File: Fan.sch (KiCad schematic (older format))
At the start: 0 parts

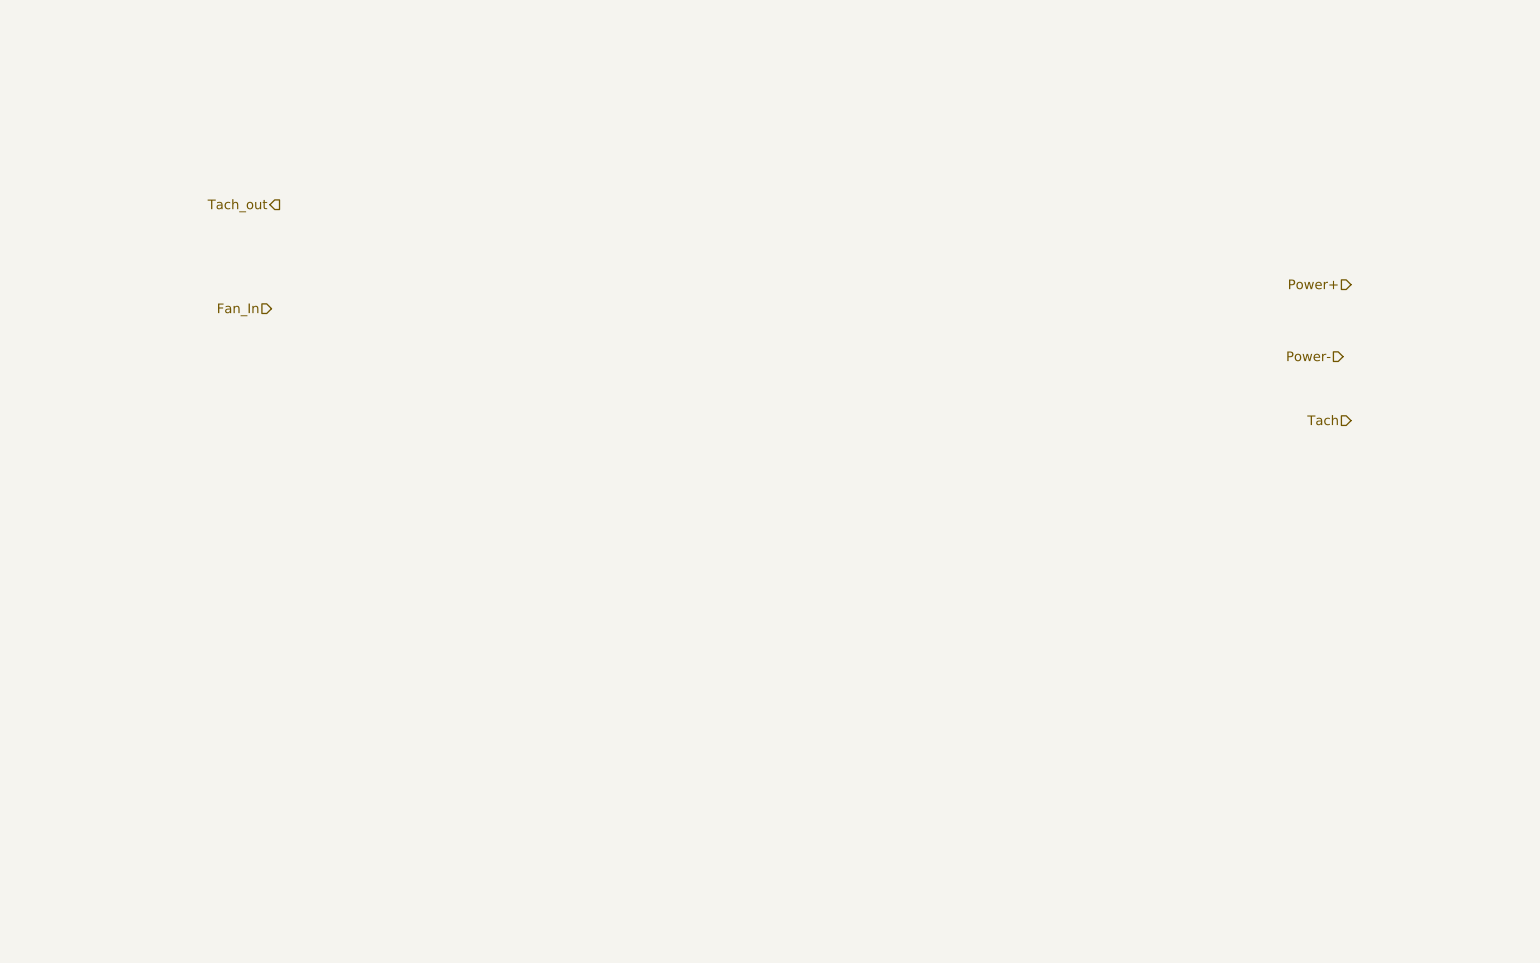
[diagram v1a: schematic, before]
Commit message: Module 3. Unit 4
Create the rough out of the Fan module
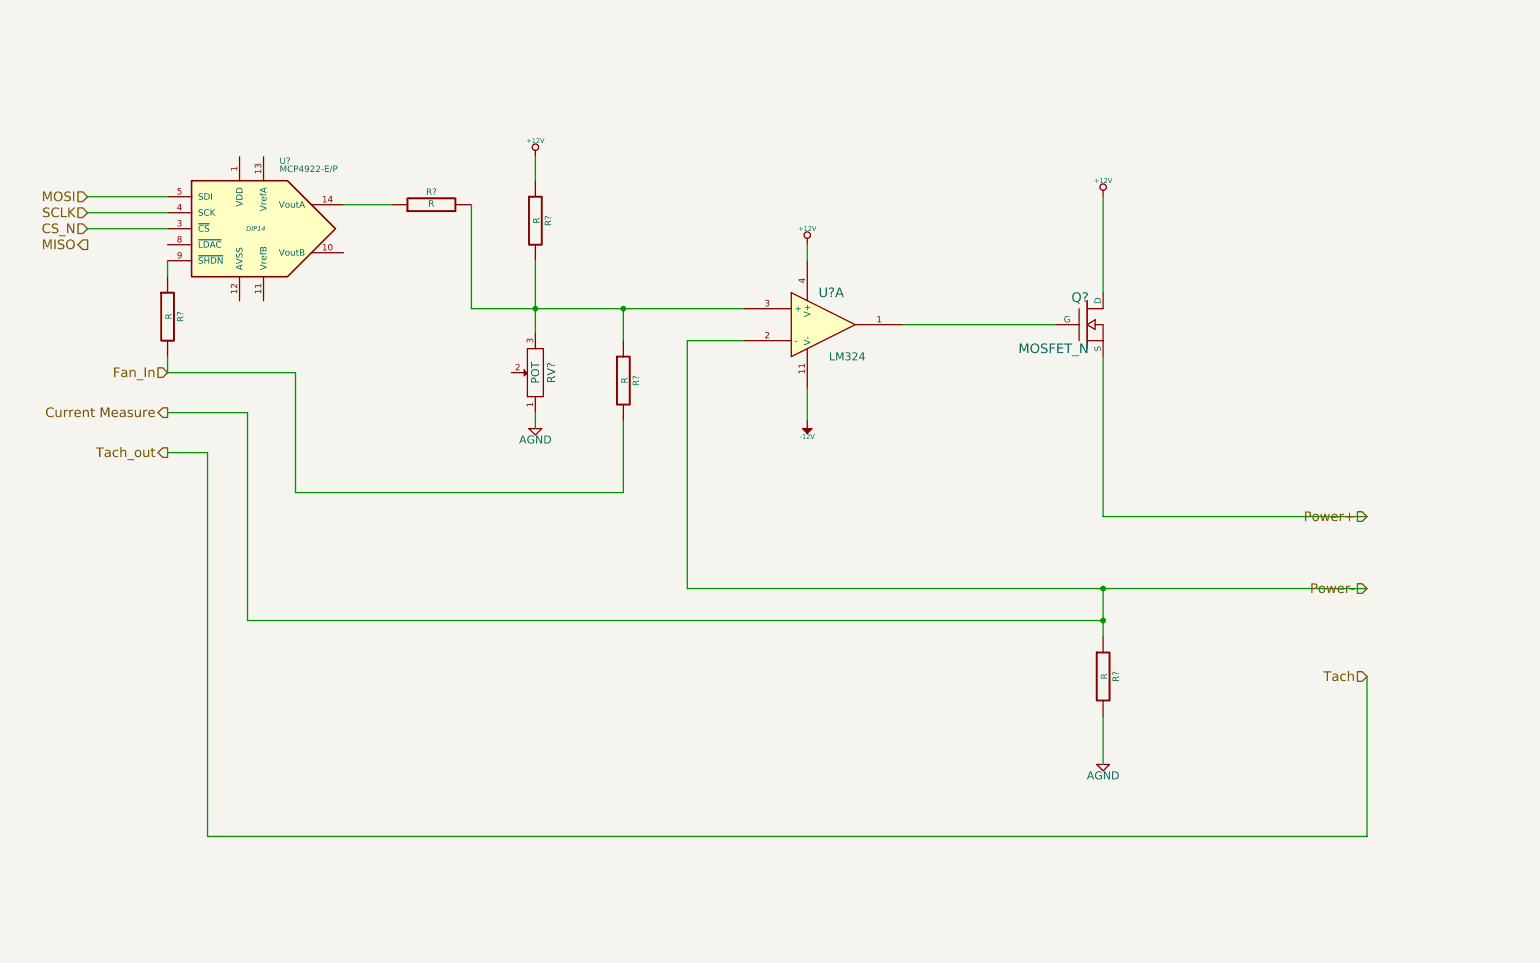
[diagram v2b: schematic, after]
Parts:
- added Q?: MOSFET_N, ~, symbol MOSFET_N
- added R? (x5): R, ~, symbol R
- added RV?: POT, ~, symbol POT
- added U?: LM324, ~, symbol LM324
- added U?: MCP4922-E/P, DIP14, symbol MCP4922-E/P
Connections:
- net Fan_In: now also R?.2, R?.2
- net Power+: now also Q?.S
- new net: Q?.G, U?.1
- new net: R?.1, R?.2, R?.2, RV?.3, U?.3 (+)
- new net: R?.1, U?.14 (VoutA)
- new net: R?.1, U?.9 (~SHDN~)
- new net +12V: Q?.D, R?.1, U?.4 (V+)
- new net -12V: U?.11 (V-)
- new net AGND: R?.2, RV?.1
- new net CS_N: U?.3 (~CS~)
- new net Current Measure: R?.1, U?.2 (-)
- new net MOSI: U?.5 (SDI)
- new net SCLK: U?.4 (SCK)

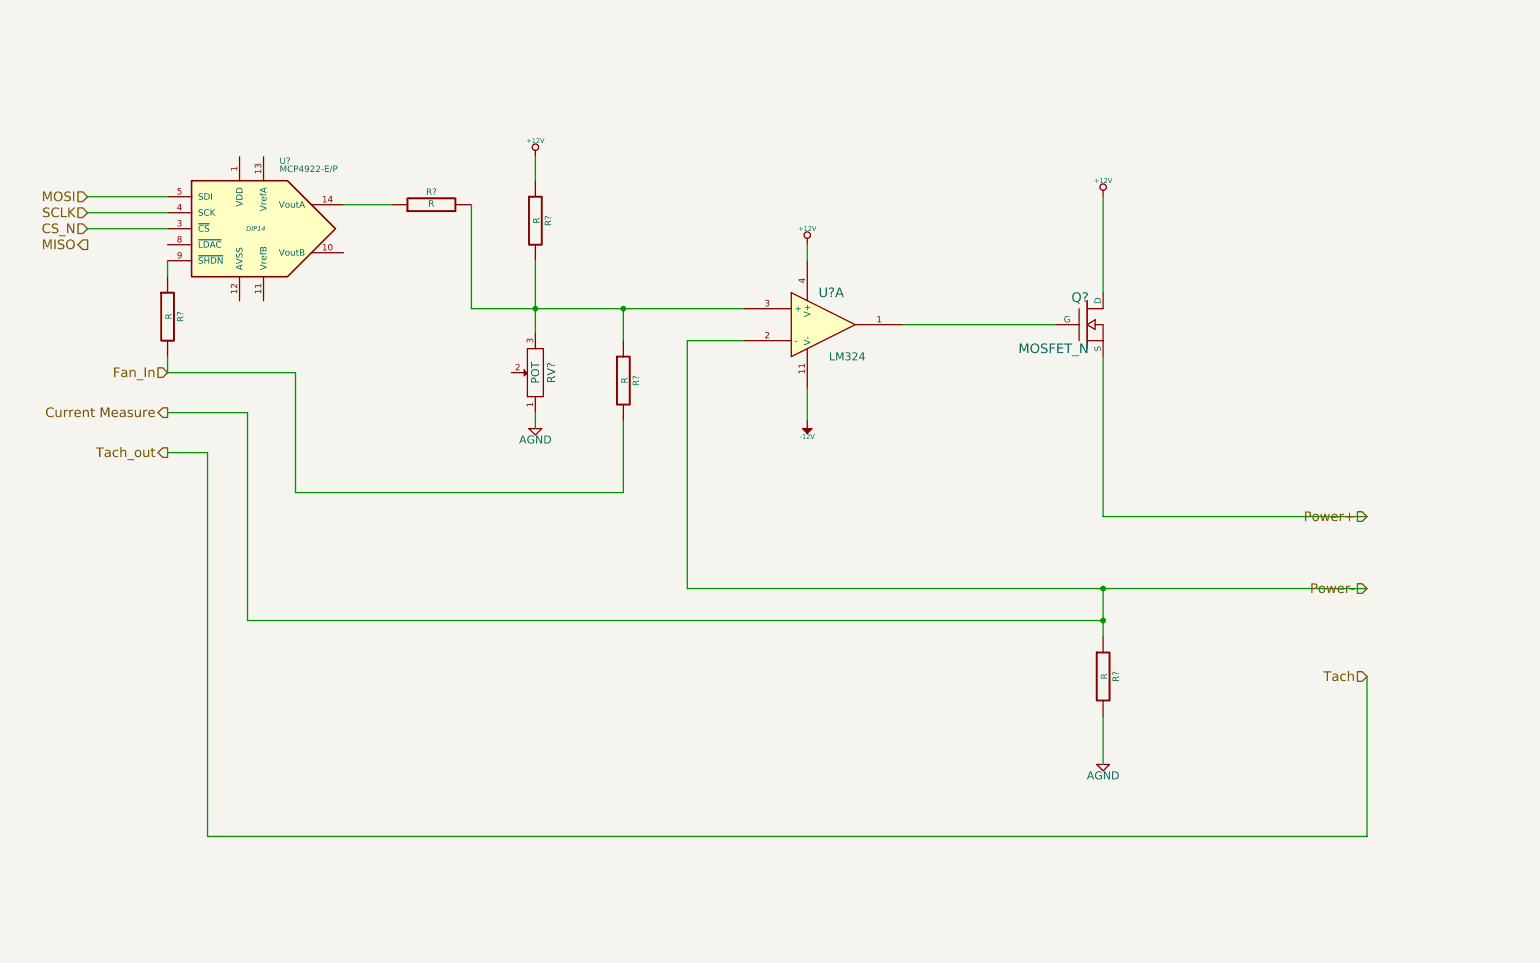
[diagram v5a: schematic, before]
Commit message: M3 U8
Arduino Module.   My Arduino Pin numbering does not matches Chris'.  I
believe he missed one in the video
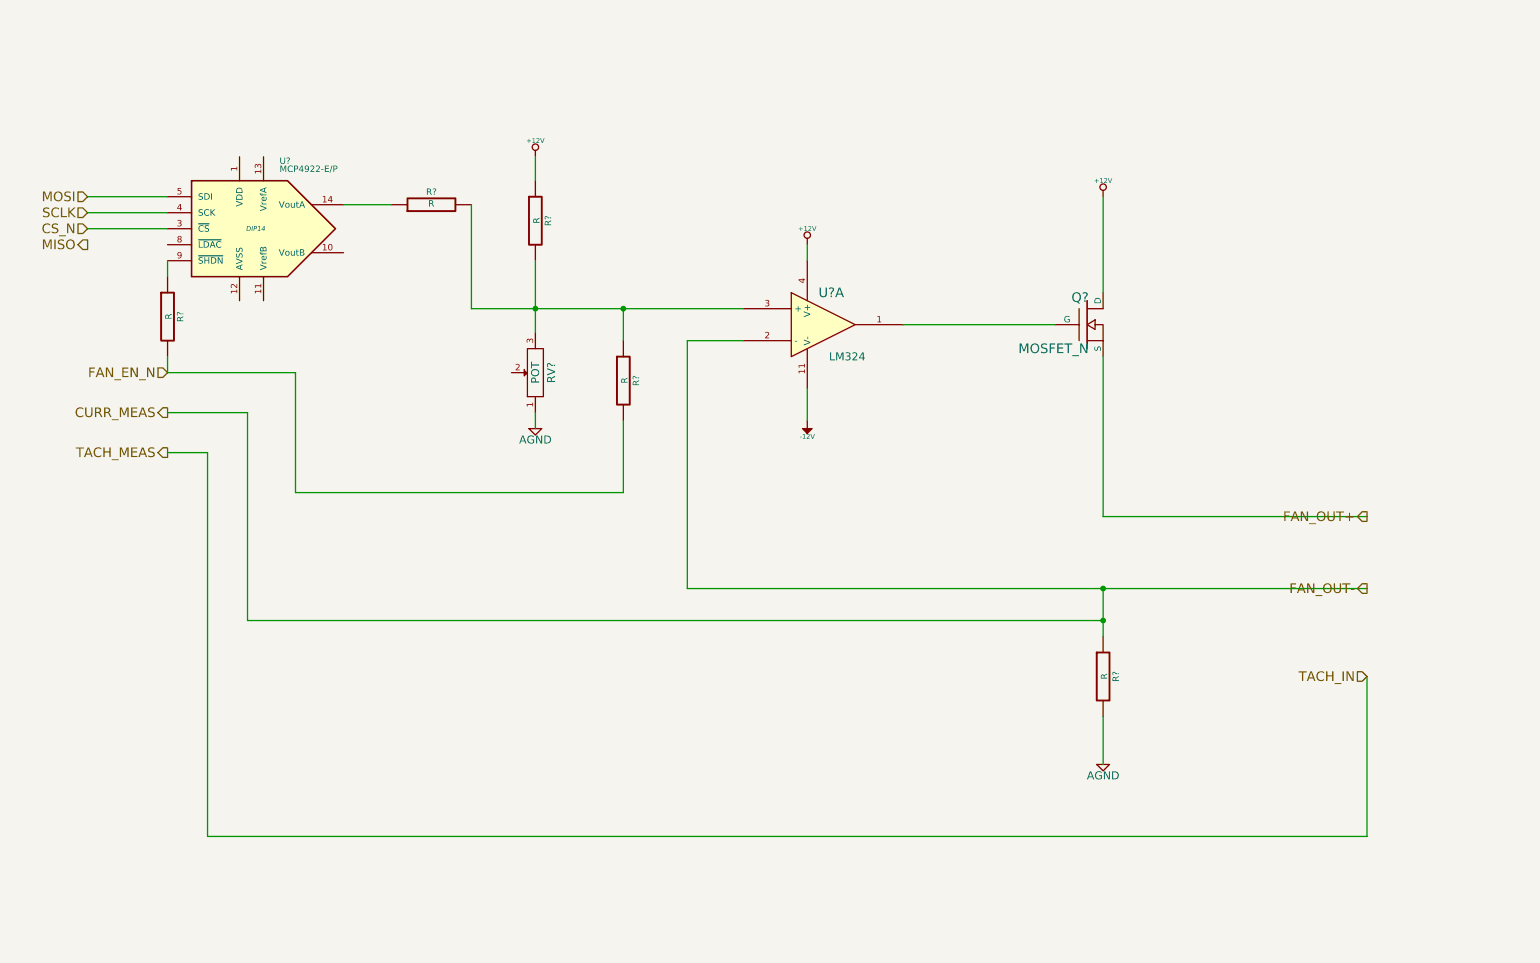
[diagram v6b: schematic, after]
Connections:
- net Current Measure renamed CURR_MEAS
- net Fan_In renamed FAN_EN_N
- net Power+ renamed FAN_OUT+
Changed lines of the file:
@@
 Sheet 7 9
 Title ""
-Date "14 feb 2014"
+Date "15 feb 2014"
 Rev ""
 Comp ""
@@
 Comment4 ""
 $EndDescr
-Text HLabel 8950 3700 0    60   Input ~ 0
-Power+
-Text HLabel 8950 4150 0    60   Input ~ 0
-Power-
+Text HLabel 8950 3700 0    60   Output ~ 0
+FAN_OUT+
+Text HLabel 8950 4150 0    60   Output ~ 0
+FAN_OUT-
 Text HLabel 8950 4700 0    60   Input ~ 0
-Tach
+TACH_IN
 Text HLabel 1450 3300 0    60   Output ~ 0
-Tach_out
+TACH_MEAS
 Text HLabel 1450 2800 0    60   Input ~ 0
-Fan_In
+FAN_EN_N
 $Comp
 L LM324 U?
@@
 	1700 5700 1700 3300
 Text HLabel 1450 3050 0    60   Output ~ 0
-Current Measure
+CURR_MEAS
 Wire Wire Line
 	7300 4350 1950 4350
